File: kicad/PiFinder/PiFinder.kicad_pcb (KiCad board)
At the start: 2 copper layers, 87.9 x 57.7 mm, 44 parts, among them J1 Raspberry_Pi_2_3, J2 display, J3 IMU, Q1 Q_NPN_EBC, SW0 SW_Push_Dual, SW1 SW_Push_Dual, SW2 SW_Push_Dual, SW3 SW_Push_Dual, SW4 SW_Push_Dual, SW5 SW_Push_Dual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

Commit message: Prep v2 case files
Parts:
- added REF**: OSHW-Logo2_14.6x12mm_SilkScreen, Symbol:OSHW-Logo2_14.6x12mm_SilkScreen, F.Cu at (108.8, 88.6)
- moved G*** 5.59 mm to (109.2, 73.3)
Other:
- board text added: "22R"
- board text added: "330R"
- board text added: "DISP1"
- board text added: "IMU1"
- board text added: "github.com/brickbots/PiFinder - PiFinder.io"

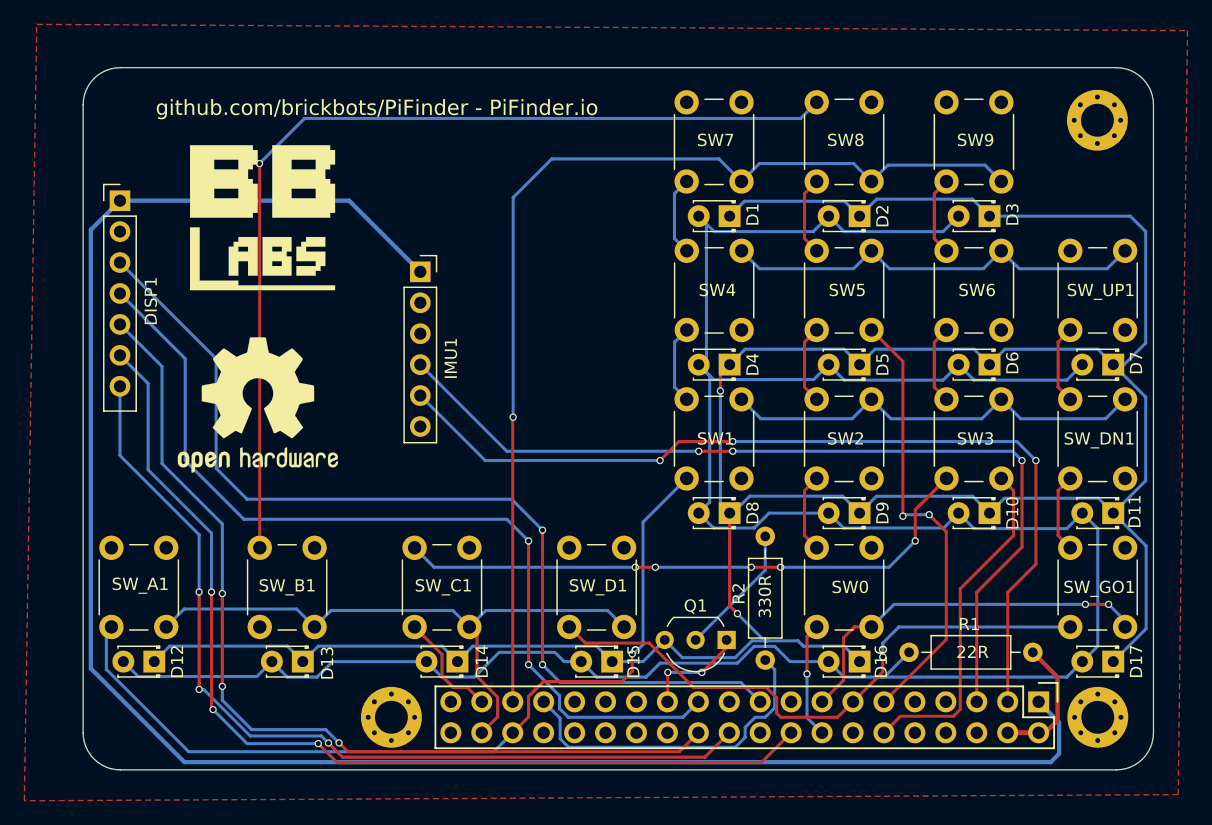
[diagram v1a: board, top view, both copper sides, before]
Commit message: Add version to PCB silkscreen
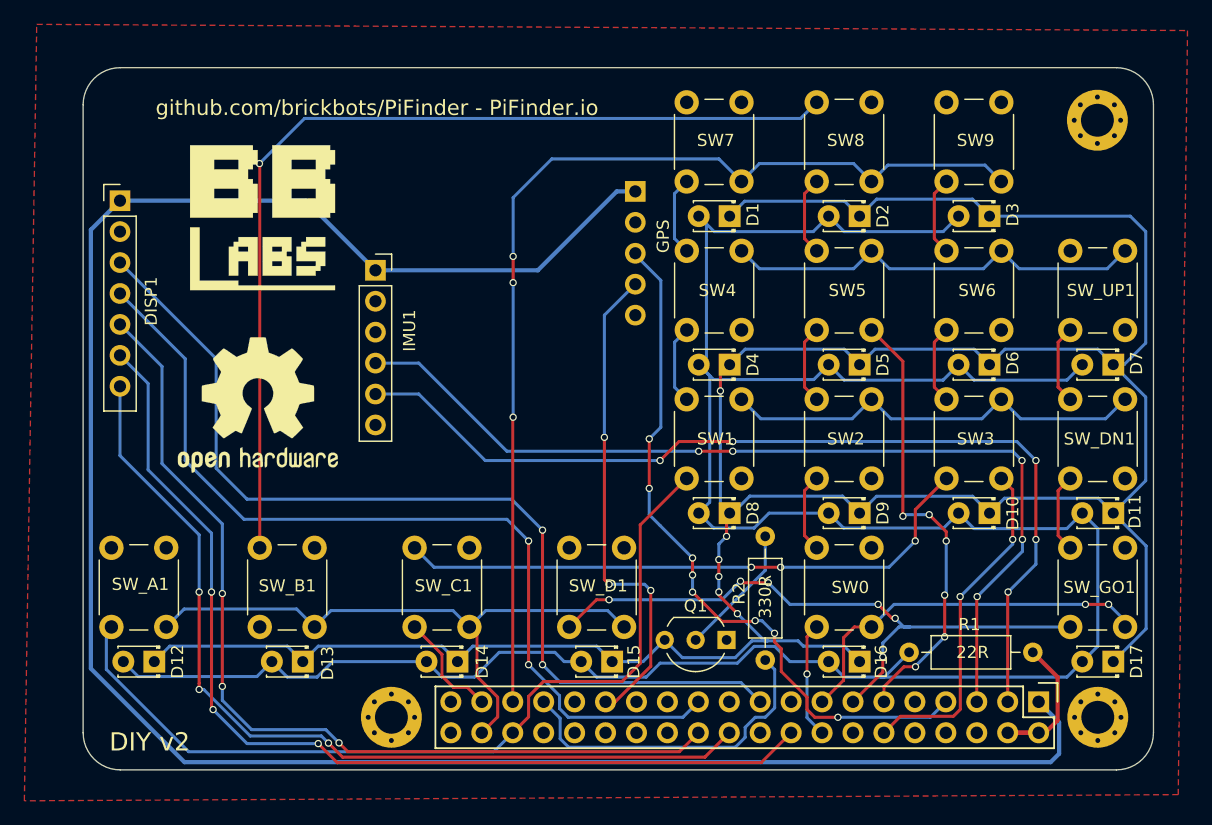
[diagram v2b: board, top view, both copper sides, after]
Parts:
- added J4: GPS Module, RSU:GT-U7_GPS, B.Cu at (139.8, 71.1)
- moved J3 3.69 mm to (118.5, 77.6)
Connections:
- J1 pad 29: unconnected-(J1-Pad29) -> UART_RX
- J1 pad 7: unconnected-(J1-Pad7) -> UART_TX
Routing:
- net UART_TX: track 0.00 -> 58.2 mm, vias 0 -> 8
- net UART_RX: track 0.00 -> 40.5 mm, vias 0 -> 3
- net +3.3V: track 154.4 -> 174.7 mm
- net GND: track 8.73 -> 0.05 mm, vias 2 -> 0
- net I2C_SCL: track 74.0 -> 77.8 mm, vias 3 -> 5
- net I2C_SDA: track 74.8 -> 78.6 mm, vias 3 -> 5
- net COL3: track 62.5 -> 65.9 mm, vias 1 -> 6
- net LED_C: track 236.1 -> 236.9 mm, vias 2 -> 6
- net ROW1: track 71.8 -> 72.3 mm, vias 2 -> 6
- net COL0: track 84.2 -> 84.1 mm, vias 1 -> 0
- net ROW2: vias 0 -> 2
- net ROW0: vias 1 -> 3
- net COL2: vias 5 -> 3
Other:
- board text added: "DIY v2"
- board text added: "GPS"

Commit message: Adding v2.5 gerbers and updated adapter for upgrades
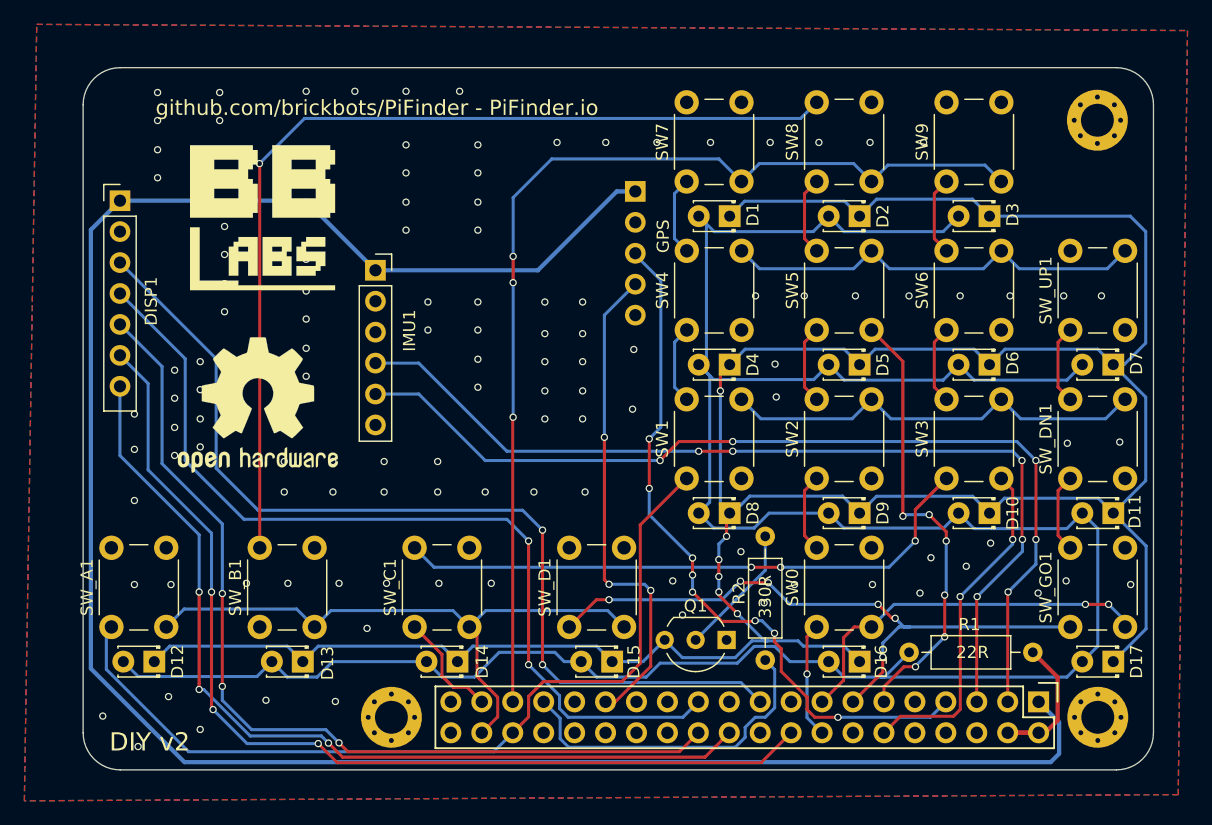
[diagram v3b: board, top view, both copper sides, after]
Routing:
- net GND: vias 0 -> 117
- added copper zone on B.Cu, net GND
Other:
- board text added: "+"
- board text added: "-"
- board text removed: "A"
- board text removed: "B"
- board text removed: "C"
- board text removed: "D"
- board text removed: "DN"
- board text removed: "ENT"
- board text removed: "UP"
